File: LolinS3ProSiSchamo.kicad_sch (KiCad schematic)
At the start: 18 parts, among them J1 OPC-XX, J2 Conn_A0, J3 Conn_A1, J4 Conn_A2, J5 Conn_A3, U1 LolinS3Pro, U2 E01-ML01DP5, U3 Adafruit Ultimate GPS, U4 BME280, U5 AdafruitADS1115, U6 MCP1700x-330xxTT, U7 AMS1117-3.3

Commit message: added qwiic connector to schematic
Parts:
- added J6, J7, J8, J9: Qwiic, MCU_Boards_Own:JST_SH_SM04B-SRSS-TB_1x04-1MP_P1.00mm_Horizontal, symbol MCU_Boards_Own:Qwiic_Connector
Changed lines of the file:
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@@
+    )
+  )
+  (symbol (lib_id "MCU_Boards_Own:Qwiic_Connector") (at 104.14 175.26 0) (unit 1)
+    (in_bom yes) (on_board yes) (dnp no) (fields_autoplaced)
+    (property "Reference" "J9" (at 107.95 181.61 0)
+      (effects (font (size 1.27 1.27)) (justify left))
+    )
+    (property "Value" "Qwiic" (at 107.95 184.15 0)
+      (effects (font (size 1.27 1.27)) (justify left))
+    )
+    (property "Footprint" "MCU_Boards_Own:JST_SH_SM04B-SRSS-TB_1x04-1MP_P1.00mm_Horizontal" (at 104.14 172.72 0)
+      (effects (font (size 1.27 1.27)) hide)
+    )
+    (property "Datasheet" "" (at 104.14 175.26 0)
+      (effects (font (size 1.27 1.27)) hide)
+    )
+    (pin "1")
+    (pin "2")
+    (pin "3")
+    (pin "4")
+    (instances
+      (project "LolinS3ProSiSchamo"
+        (path "/57bdba71-8370-4839-a707-08eb67ebb58d"
+          (reference "J9") (unit 1)
+        )
+      )
     )
   )
@@
     )
   )
+  (symbol (lib_id "MCU_Boards_Own:Qwiic_Connector") (at 87.63 175.26 0) (unit 1)
+    (in_bom yes) (on_board yes) (dnp no) (fields_autoplaced)
+    (property "Reference" "J8" (at 91.44 181.61 0)
+      (effects (font (size 1.27 1.27)) (justify left))
+    )
+    (property "Value" "Qwiic" (at 91.44 184.15 0)
+      (effects (font (size 1.27 1.27)) (justify left))
+    )
+    (property "Footprint" "MCU_Boards_Own:JST_SH_SM04B-SRSS-TB_1x04-1MP_P1.00mm_Horizontal" (at 87.63 172.72 0)
+      (effects (font (size 1.27 1.27)) hide)
+    )
+    (property "Datasheet" "" (at 87.63 175.26 0)
+      (effects (font (size 1.27 1.27)) hide)
+    )
+    (pin "1")
+    (pin "2")
+    (pin "3")
+    (pin "4")
+    (instances
+      (project "LolinS3ProSiSchamo"
+        (path "/57bdba71-8370-4839-a707-08eb67ebb58d"
+          (reference "J8") (unit 1)
+        )
+      )
+    )
+  )
   (symbol (lib_id "power:GND") (at 34.29 109.22 0) (unit 1)
     (in_bom yes) (on_board yes) (dnp no) (fields_autoplaced)
@@
         )
       )
+    )
+  )
+  (symbol (lib_id "MCU_Boards_Own:Qwiic_Connector") (at 55.88 175.26 0) (unit 1)
+    (in_bom yes) (on_board yes) (dnp no) (fields_autoplaced)
+    (property "Reference" "J6" (at 59.69 181.61 0)
+      (effects (font (size 1.27 1.27)) (justify left))
+    )
+    (property "Value" "Qwiic" (at 59.69 184.15 0)
+      (effects (font (size 1.27 1.27)) (justify left))
+    )
+    (property "Footprint" "MCU_Boards_Own:JST_SH_SM04B-SRSS-TB_1x04-1MP_P1.00mm_Horizontal" (at 55.88 172.72 0)
+      (effects (font (size 1.27 1.27)) hide)
+    )
+    (property "Datasheet" "" (at 55.88 175.26 0)
+      (effects (font (size 1.27 1.27)) hide)
+    )
+    (pin "1")
+    (pin "2")
+    (pin "3")
+    (pin "4")
+    (instances
+      (project "LolinS3ProSiSchamo"
+        (path "/57bdba71-8370-4839-a707-08eb67ebb58d"
+          (reference "J6") (unit 1)
+        )
+      )
+    )
+  )
+  (symbol (lib_id "MCU_Boards_Own:Qwiic_Connector") (at 71.12 175.26 0) (unit 1)
+    (in_bom yes) (on_board yes) (dnp no) (fields_autoplaced)
+    (property "Reference" "J7" (at 74.93 181.61 0)
+      (effects (font (size 1.27 1.27)) (justify left))
+    )
+    (property "Value" "Qwiic" (at 74.93 184.15 0)
+      (effects (font (size 1.27 1.27)) (justify left))
+    )
+    (property "Footprint" "MCU_Boards_Own:JST_SH_SM04B-SRSS-TB_1x04-1MP_P1.00mm_Horizontal" (at 71.12 172.72 0)
+      (effects (font (size 1.27 1.27)) hide)
+    )
+    (property "Datasheet" "" (at 71.12 175.26 0)
+      (effects (font (size 1.27 1.27)) hide)
+    )
+    (pin "1")
+    (pin "2")
+    (pin "3")
+    (pin "4")
+    (instances
+      (project "LolinS3ProSiSchamo"
+        (path "/57bdba71-8370-4839-a707-08eb67ebb58d"
+          (reference "J7") (unit 1)
+        )
+      )

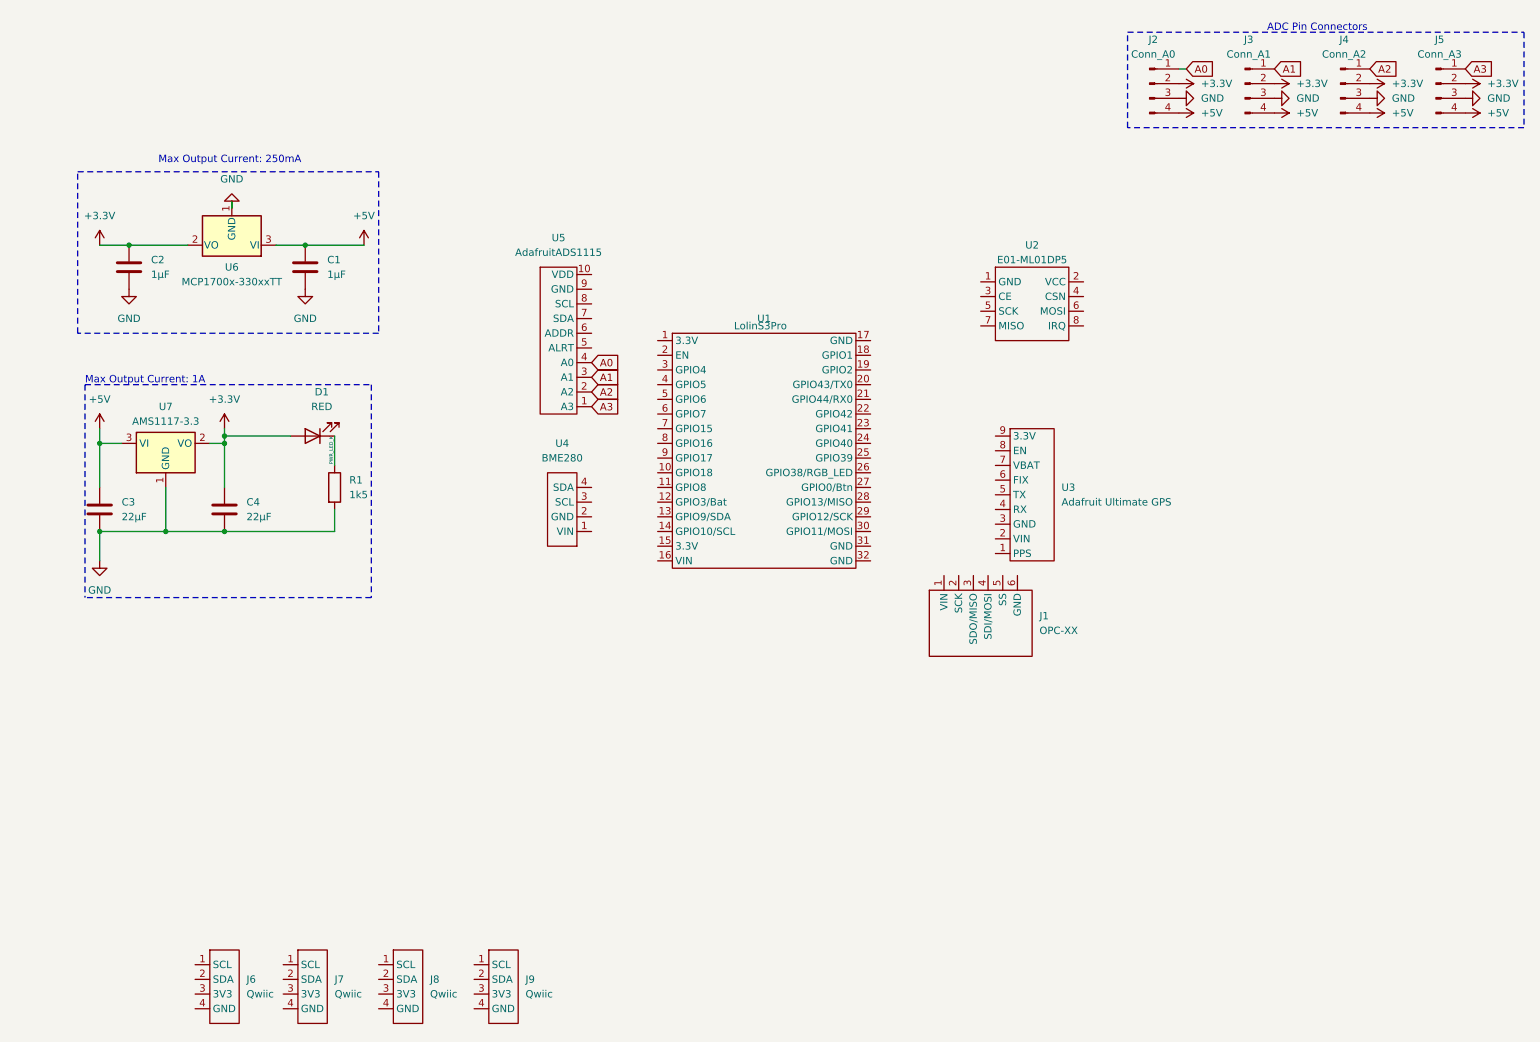
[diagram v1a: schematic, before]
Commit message: component connections added
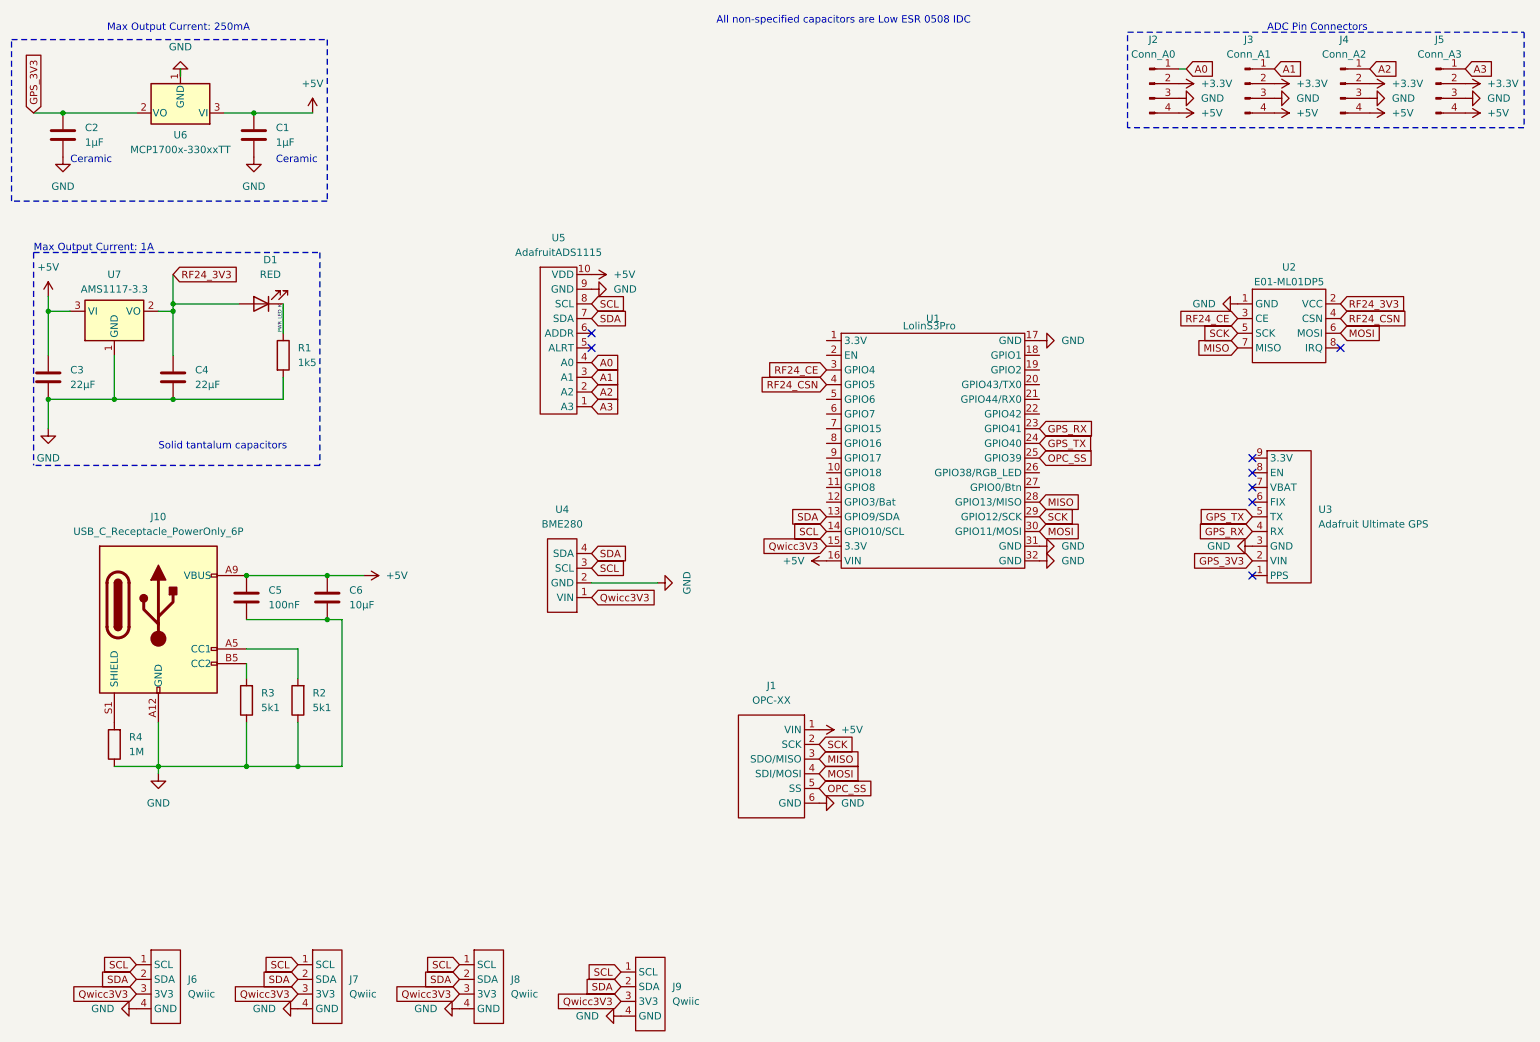
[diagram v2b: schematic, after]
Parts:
- added C5: 100nF, symbol Device:C
- added C6: 10µF, symbol Device:C
- added J10: USB_C_Receptacle_PowerOnly_6P, Connector_USB:USB_C_Receptacle_GCT_USB4135-GF-A_6P_TopMnt_Horizontal, symbol Connector:USB_C_Receptacle_PowerOnly_6P
- added R2, R3: 5k1, symbol Device:R
- added R4: 1M, symbol Device:R
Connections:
- net +3.3V: no longer C2.1, C4.1, D1.2 (A), U6.2 (VO), U7.2 (VO)
- net +5V: now also J1.1 (VIN), U1.16 (VIN), U5.10 (VDD), C5.1, C6.1, J10.A9 (VBUS), J10.B9 (VBUS)
- net GND: now also J1.6 (GND), J6.4 (GND), J7.4 (GND), J8.4 (GND), J9.4 (GND), U1.17 (GND), U1.31 (GND), U1.32 (GND), U2.1 (GND), U3.3 (GND), U4.2 (GND), U5.9 (GND), C5.2, C6.2, J10.A12 (GND), J10.B12 (GND), R2.1, R3.1, R4.1
- net SDA: now reaches U5.7 (SDA)
- net SDA: now also J6.2 (SDA), J7.2 (SDA), J8.2 (SDA), J9.2 (SDA), U1.13 (GPIO9/SDA), U4.4 (SDA)
- net SCL: now reaches U5.8 (SCL)
- net SCL: now also J6.1 (SCL), J7.1 (SCL), J8.1 (SCL), J9.1 (SCL), U1.14 (GPIO10/SCL), U4.3 (SCL)
- net Qwicc3V3: now reaches J9.3 (3V3)
- net Qwicc3V3: now also J6.3 (3V3), J7.3 (3V3), J8.3 (3V3), U1.15 (3.3V), U4.1 (VIN)
- net GPS_RX: now reaches U1.23 (GPIO41)
- net GPS_RX: now also U3.4 (RX)
- net GPS_TX: now reaches U1.24 (GPIO40)
- net GPS_TX: now also U3.5 (TX)
- net OPC_SS: now reaches U1.25 (GPIO39)
- net OPC_SS: now also J1.5 (SS)
- net MISO: now reaches U1.28 (GPIO13/MISO)
- net MISO: now also J1.3 (SDO/MISO), U2.7 (MISO)
- net SCK: now reaches U1.29 (GPIO12/SCK)
- net SCK: now also J1.2 (SCK), U2.5 (SCK)
- net RF24_CE: now reaches U1.3 (GPIO4)
- net RF24_CE: now also U2.3 (CE)
- net MOSI: now reaches U1.30 (GPIO11/MOSI)
- net MOSI: now also J1.4 (SDI/MOSI), U2.6 (MOSI)
- net RF24_CSN: now reaches U1.4 (GPIO5)
- net RF24_CSN: now also U2.4 (CSN)
- net RF24_3V3: now reaches U2.2 (VCC)
- net RF24_3V3: now also C4.1, D1.2 (A), U7.2 (VO)
- net GPS_3V3: now reaches U3.2 (VIN)
- net GPS_3V3: now also C2.1, U6.2 (VO)
- new net: J10.A5 (CC1), R2.2
- new net: J10.B5 (CC2), R3.2
- new net: J10.S1 (SHIELD), R4.2
- no-connect marks 0 -> 8
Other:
- note added: "All non-specified capacitors are Low ESR 0508 IDC"
- note added: "Ceramic"
- note added: "Solid tantalum capacitors"
- company: (none) -> https://github.com/SiSchaMoHSD/Lolin-S3-Pro_Air_PCB
- title: (none) -> SiSchaMo PCB WemosS3Pro
- moved on the sheet: C1, C2, C3, C4, D1, J1, J6, J7, J8, J9, R1, U1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
